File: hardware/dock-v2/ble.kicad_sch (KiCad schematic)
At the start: 13 parts, among them U501 ESP32-C3-MINI-1-H4X

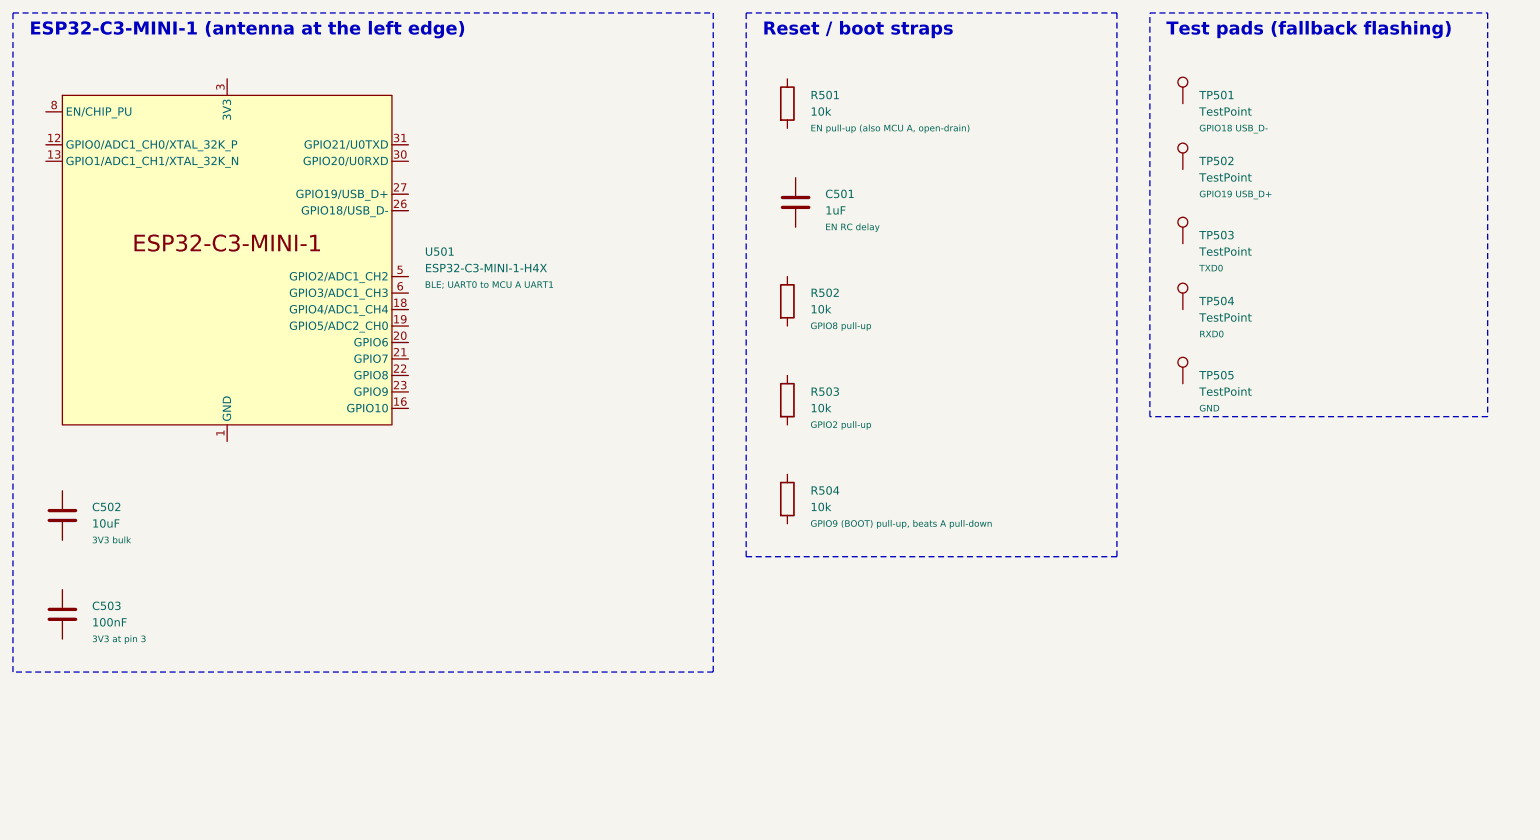
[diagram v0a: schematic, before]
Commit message: Dock v2 schematic: wiring in progress (user's work, snapshot before fixes)
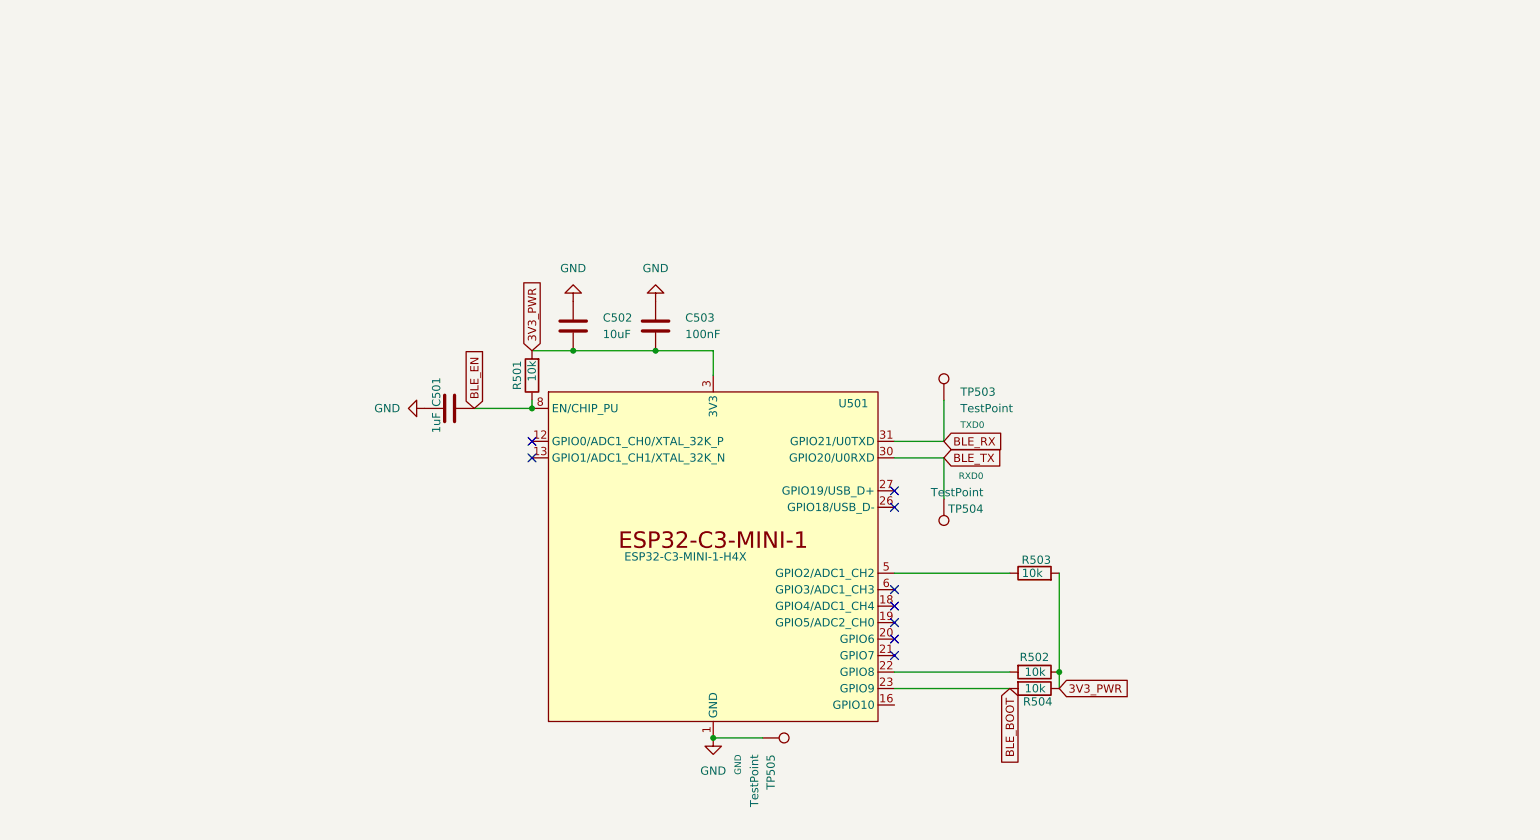
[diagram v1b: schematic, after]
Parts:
- removed TP501, TP502: TestPoint, TestPoint:TestPoint_Pad_D1.0mm, symbol Connector:TestPoint
- R504: Note GPIO9 (BOOT) pull-up, beats A pull-down -> GPIO2 pull-up
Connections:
- net GND: now reaches C501.1
- net GND: now also C502.1, C503.1, TP505.1, U501.1 (GND), U501.11 (GND), U501.14 (GND), U501.2 (GND), U501.36 (GND), U501.37 (GND), U501.38 (GND), U501.39 (GND), U501.40 (GND), U501.41 (GND), U501.42 (GND), U501.43 (GND), U501.44 (GND), U501.45 (GND), U501.46 (GND), U501.47 (GND), U501.48 (GND), U501.49 (GND), U501.50 (GND), U501.51 (GND), U501.52 (GND), U501.53 (GND)
- net BLE_EN: now reaches C501.2
- net BLE_EN: now also R501.1, U501.8 (EN/CHIP_PU)
- net 3V3_PWR: now reaches R502.1
- net 3V3_PWR: now also C502.2, C503.2, R501.2, R503.2, R504.1, U501.3 (3V3)
- net at R502.2: now also U501.22 (GPIO8)
- net BLE_RX: now reaches TP503.1
- net BLE_RX: now also U501.31 (GPIO21/U0TXD)
- net at R503.1: now also U501.5 (GPIO2/ADC1_CH2)
- net BLE_BOOT: now reaches R504.2
- net BLE_BOOT: now also U501.23 (GPIO9)
- net BLE_TX: now reaches TP504.1
- net BLE_TX: now also U501.30 (GPIO20/U0RXD)
- no-connect marks 0 -> 9
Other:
- note removed: "ESP32-C3-MINI-1 (antenna at the left edge)"
- note removed: "Reset / boot straps"
- note removed: "Test pads (fallback flashing)"
